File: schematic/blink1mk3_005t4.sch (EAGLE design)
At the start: 18 parts, among them T0A TPTP15R, T1B TPTP15R, U1 EFM32HG309F64G, X1 USB

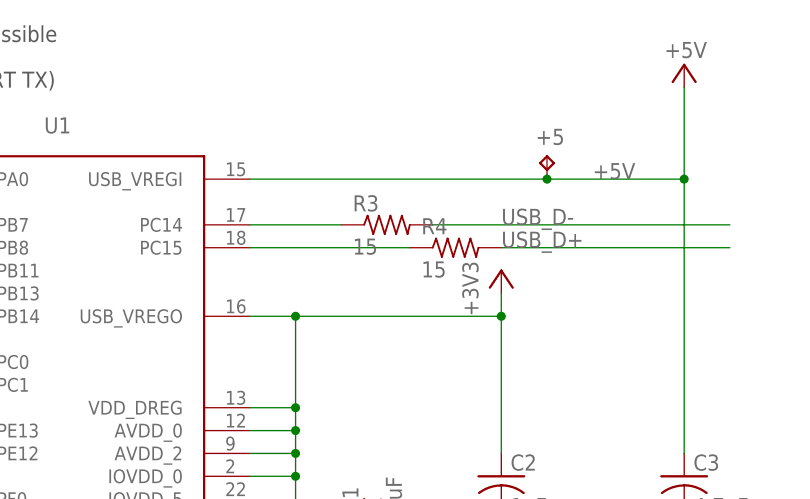
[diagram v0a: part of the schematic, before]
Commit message: small blink1 mk3 schematic fixes before release to manufacturing
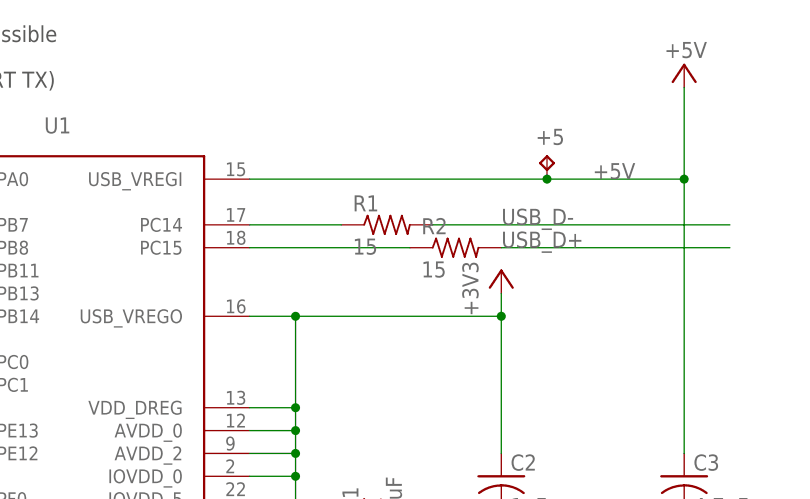
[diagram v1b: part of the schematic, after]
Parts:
- renumbered R3 to R1, R4 to R2
